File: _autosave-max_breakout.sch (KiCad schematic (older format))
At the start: 44 parts, among them J1 Left, J2 Right, J3 AVR-JTAG-10, J4 USB_B_Micro, Q1 IRLML6402, SW1 Reset, SW2 User, SW3 User DIP Switch, SW4 ENA Switch, U1 AP7381-33SA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

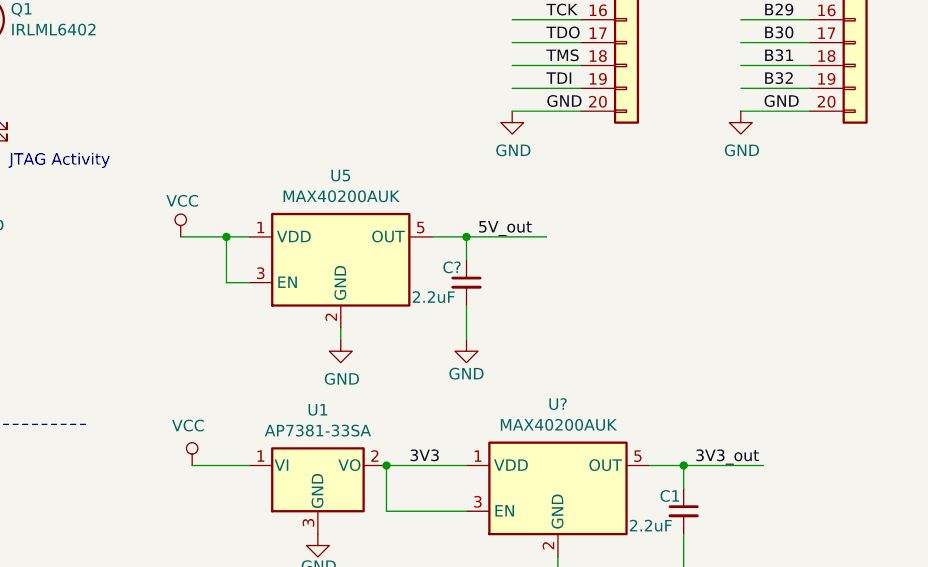
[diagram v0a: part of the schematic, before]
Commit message: changed 20pin headers
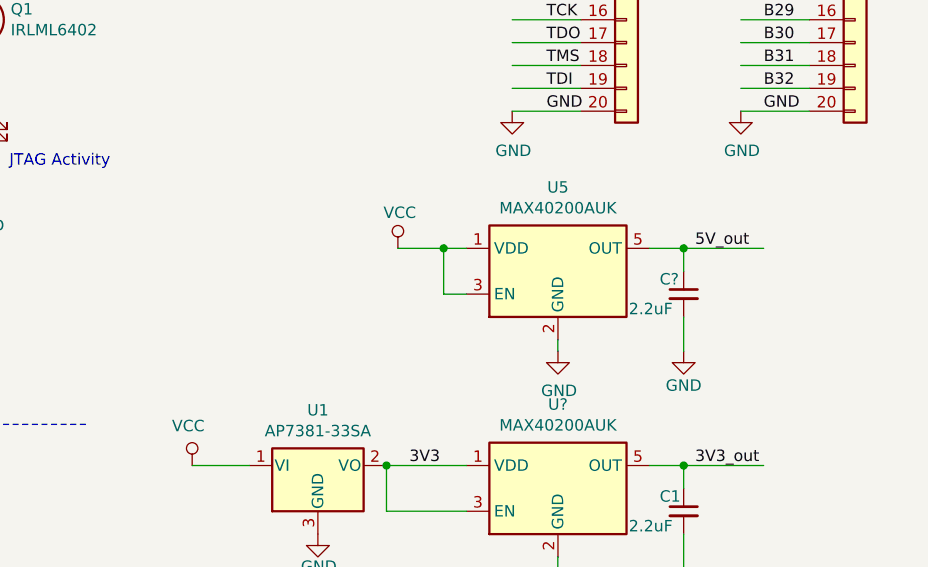
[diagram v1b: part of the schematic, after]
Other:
- moved on the sheet: C?, U5
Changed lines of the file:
@@
 L power:GND #PWR028
 U 1 1 5D385EAD
-P 8150 3550
+P 9100 3600
 AR Path="/5D385EAD" Ref="#PWR028"  Part="1"
 AR Path="/5CB63856/5D385EAD" Ref="#PWR?"  Part="1"
@@
 AR Path="/5D0F9837/5D385EAD" Ref="#PWR?"  Part="1"
 AR Path="/5CFABACD/5D0BF766/5D385EAD" Ref="#PWR?"  Part="1"
-F 0 "#PWR028" H 8150 3300 50  0001 C CNN
-F 1 "GND" H 8155 3377 50  0000 C CNN
-F 2 "" H 8150 3550 50  0001 C CNN
-F 3 "" H 8150 3550 50  0001 C CNN
-	1    8150 3550
+F 0 "#PWR028" H 9100 3350 50  0001 C CNN
+F 1 "GND" H 9105 3427 50  0000 C CNN
+F 2 "" H 9100 3600 50  0001 C CNN
+F 3 "" H 9100 3600 50  0001 C CNN
+	1    9100 3600
 	1    0    0    -1
 $EndComp
@@
 L max_breakout-rescue:MAX40200AUK-Analog_Switch U5
 U 1 1 5D385EAE
-P 8150 3200
-F 0 "U5" H 8150 3567 50  0000 C CNN
-F 1 "MAX40200AUK" H 8150 3476 50  0000 C CNN
-F 2 "Package_TO_SOT_SMD:SOT-23-5_HandSoldering" H 8150 3700 50  0001 C CNN
-F 3 "https://www.mouser.com/datasheet/2/256/MAX40200-1112995.pdf" H 8150 3700 50  0001 C CNN
-F 4 "https://www.mouser.com/datasheet/2/256/MAX40200-1112995.pdf" H 8150 3667 50  0001 C CNN "Datasheet"
-F 5 "Supervisory Circuits Current Sense/Ideal Diode" H 8150 3667 50  0001 C CNN "Description"
-F 6 "Package_TO_SOT_SMD:SOT-23-5_HandSoldering" H 8150 3667 50  0001 C CNN "Footprint"
-F 7 "Maxim" H 8150 3667 50  0001 C CNN "MFR"
-F 8 "MAX40200AUK+T" H 8150 3667 50  0001 C CNN "MPN"
-F 9 "700-MAX40200AUK+T" H 8150 3667 50  0001 C CNN "SPN"
-F 10 "Mouser" H 8150 3667 50  0001 C CNN "SPR"
-F 11 "https://www.mouser.com/ProductDetail/Maxim-Integrated/MAX40200AUK%2BT?qs=5aG0NVq1C4yORXmgClGWGQ%3D%3D&gclid=Cj0KCQjwho7rBRDxARIsAJ5nhFrTlEoNuSrU5Ut2EFDDcmbkuDqplPKK4X4qR73RchZcKA7ftlt8MIYaAsf8EALw_wcB" H 8150 3667 50  0001 C CNN "SPURL"
-F 12 "MAX40200AUK" H 8150 3667 50  0001 C CNN "Value"
-	1    8150 3200
+P 9100 3250
+F 0 "U5" H 9100 3617 50  0000 C CNN
+F 1 "MAX40200AUK" H 9100 3526 50  0000 C CNN
+F 2 "Package_TO_SOT_SMD:SOT-23-5_HandSoldering" H 9100 3750 50  0001 C CNN
+F 3 "https://www.mouser.com/datasheet/2/256/MAX40200-1112995.pdf" H 9100 3750 50  0001 C CNN
+F 4 "https://www.mouser.com/datasheet/2/256/MAX40200-1112995.pdf" H 9100 3717 50  0001 C CNN "Datasheet"
+F 5 "Supervisory Circuits Current Sense/Ideal Diode" H 9100 3717 50  0001 C CNN "Description"
+F 6 "Package_TO_SOT_SMD:SOT-23-5_HandSoldering" H 9100 3717 50  0001 C CNN "Footprint"
+F 7 "Maxim" H 9100 3717 50  0001 C CNN "MFR"
+F 8 "MAX40200AUK+T" H 9100 3717 50  0001 C CNN "MPN"
+F 9 "700-MAX40200AUK+T" H 9100 3717 50  0001 C CNN "SPN"
+F 10 "Mouser" H 9100 3717 50  0001 C CNN "SPR"
+F 11 "https://www.mouser.com/ProductDetail/Maxim-Integrated/MAX40200AUK%2BT?qs=5aG0NVq1C4yORXmgClGWGQ%3D%3D&gclid=Cj0KCQjwho7rBRDxARIsAJ5nhFrTlEoNuSrU5Ut2EFDDcmbkuDqplPKK4X4qR73RchZcKA7ftlt8MIYaAsf8EALw_wcB" H 9100 3717 50  0001 C CNN "SPURL"
+F 12 "MAX40200AUK" H 9100 3717 50  0001 C CNN "Value"
+	1    9100 3250
 	1    0    0    -1
 $EndComp
@@
 L power:VCC #PWR019
 U 1 1 5DD7F47B
-P 7450 3100
-F 0 "#PWR019" H 7450 2950 50  0001 C CNN
-F 1 "VCC" H 7458 3256 50  0000 C CNN
-F 2 "" H 7450 3100 50  0001 C CNN
-F 3 "" H 7450 3100 50  0001 C CNN
-	1    7450 3100
+P 8400 3150
+F 0 "#PWR019" H 8400 3000 50  0001 C CNN
+F 1 "VCC" H 8408 3306 50  0000 C CNN
+F 2 "" H 8400 3150 50  0001 C CNN
+F 3 "" H 8400 3150 50  0001 C CNN
+	1    8400 3150
 	1    0    0    -1
 $EndComp
@@
 	8600 5200 8700 5200
 Wire Wire Line
-	7750 3300 7650 3300
-Wire Wire Line
-	7650 3300 7650 3100
-Wire Wire Line
-	7650 3100 7450 3100
+	8700 3350 8600 3350
+Wire Wire Line
+	8600 3350 8600 3150
+Wire Wire Line
+	8600 3150 8400 3150
 Wire Wire Line
 	9650 5050 9650 5200
 Wire Wire Line
-	7750 3100 7650 3100
+	8700 3150 8600 3150
 Wire Wire Line
 	7950 1850 7950 1800
@@
 	550  1350 750  1350
 Wire Wire Line
-	8150 3550 8150 3500
+	9100 3600 9100 3550
 Wire Wire Line
 	2850 3600 2850 3700
@@
 Connection ~ 8150 1800
 Connection ~ 8600 5200
-Connection ~ 7650 3100
+Connection ~ 8600 3150
 Connection ~ 8100 6100
 Connection ~ 7750 1800
@@
 L Device:C_Small C?
 U 1 1 5DABCD39
-P 8700 3300
+P 9650 3350
 AR Path="/5D65A6A0/5DABCD39" Ref="C?"  Part="1"
 AR Path="/5DABCD39" Ref="C?"  Part="1"
-F 0 "C?" H 8595 3365 50  0000 L CNN
-F 1 "2.2uF" H 8460 3235 50  0000 L CNN
-F 2 "Capacitor_SMD:C_0603_1608Metric_Pad1.05x0.95mm_HandSolder" H 8700 3300 50  0001 C CNN
-F 3 "https://www.mouser.com/datasheet/2/396/mlcc02_e-1307760.pdf" H 8700 3300 50  0001 C CNN
-F 4 "https://www.mouser.com/datasheet/2/396/mlcc02_e-1307760.pdf" H 8595 3465 50  0001 C CNN "Datasheet"
-F 5 "Multilayer Ceramic Capacitors MLCC - SMD/SMT 0603 6.3V 2.2uF 10% X7R" H 8792 3446 50  0001 C CNN "Description"
-F 6 "Capacitor_SMD:C_0603_1608Metric_Pad1.05x0.95mm_HandSolder" H 8595 3465 50  0001 C CNN "Footprint"
-F 7 "Murata" H 8700 3300 50  0001 C CNN "MFR"
-F 8 "JMK107B7474KA-T" H 8700 3300 50  0001 C CNN "MPN"
-F 9 "963-JMK107B7474KA-T" H 8792 3446 50  0001 C CNN "SPN"
-F 10 "Mouser" H 8700 3300 50  0001 C CNN "SPR"
-F 11 "https://www.mouser.com/ProductDetail/963-JMK107B7474KA-T" H 8792 3446 50  0001 C CNN "SPURL"
-F 12 "2.2uF" H 8595 3465 50  0001 C CNN "Value"
-	1    8700 3300
+F 0 "C?" H 9545 3415 50  0000 L CNN
+F 1 "2.2uF" H 9410 3285 50  0000 L CNN
+F 2 "Capacitor_SMD:C_0603_1608Metric_Pad1.05x0.95mm_HandSolder" H 9650 3350 50  0001 C CNN
+F 3 "https://www.mouser.com/datasheet/2/396/mlcc02_e-1307760.pdf" H 9650 3350 50  0001 C CNN
+F 4 "https://www.mouser.com/datasheet/2/396/mlcc02_e-1307760.pdf" H 9545 3515 50  0001 C CNN "Datasheet"
+F 5 "Multilayer Ceramic Capacitors MLCC - SMD/SMT 0603 6.3V 2.2uF 10% X7R" H 9742 3496 50  0001 C CNN "Description"
+F 6 "Capacitor_SMD:C_0603_1608Metric_Pad1.05x0.95mm_HandSolder" H 9545 3515 50  0001 C CNN "Footprint"
+F 7 "Murata" H 9650 3350 50  0001 C CNN "MFR"
+F 8 "JMK107B7474KA-T" H 9650 3350 50  0001 C CNN "MPN"
+F 9 "963-JMK107B7474KA-T" H 9742 3496 50  0001 C CNN "SPN"
+F 10 "Mouser" H 9650 3350 50  0001 C CNN "SPR"
+F 11 "https://www.mouser.com/ProductDetail/963-JMK107B7474KA-T" H 9742 3496 50  0001 C CNN "SPURL"
+F 12 "2.2uF" H 9545 3515 50  0001 C CNN "Value"
+	1    9650 3350
 	1    0    0    -1
 $EndComp
@@
 L power:GND #PWR?
 U 1 1 5DABCD3F
-P 8700 3550
+P 9650 3600
 AR Path="/5DABCD3F" Ref="#PWR?"  Part="1"
 AR Path="/5CB63856/5DABCD3F" Ref="#PWR?"  Part="1"
@@
 AR Path="/5D0F9837/5DABCD3F" Ref="#PWR?"  Part="1"
 AR Path="/5CFABACD/5D0BF766/5DABCD3F" Ref="#PWR?"  Part="1"
-F 0 "#PWR?" H 8700 3300 50  0001 C CNN
-F 1 "GND" H 8700 3400 50  0000 C CNN
-F 2 "" H 8700 3550 50  0001 C CNN
-F 3 "" H 8700 3550 50  0001 C CNN
-	1    8700 3550
-	1    0    0    -1
-$EndComp
-Wire Wire Line
-	8700 3400 8700 3550
-Wire Wire Line
-	8700 3200 8700 3100
-Wire Wire Line
-	8700 3100 8550 3100
-Wire Wire Line
-	8700 3100 9050 3100
-Connection ~ 8700 3100
-Text Label 8750 3100 0    50   ~ 0
+F 0 "#PWR?" H 9650 3350 50  0001 C CNN
+F 1 "GND" H 9650 3450 50  0000 C CNN
+F 2 "" H 9650 3600 50  0001 C CNN
+F 3 "" H 9650 3600 50  0001 C CNN
+	1    9650 3600
+	1    0    0    -1
+$EndComp
+Wire Wire Line
+	9650 3450 9650 3600
+Wire Wire Line
+	9650 3250 9650 3150
+Wire Wire Line
+	9650 3150 9500 3150
+Wire Wire Line
+	9650 3150 10000 3150
+Connection ~ 9650 3150
+Text Label 9700 3150 0    50   ~ 0
 5V_out
 Wire Wire Line
